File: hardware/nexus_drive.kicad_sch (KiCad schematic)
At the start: 0 parts

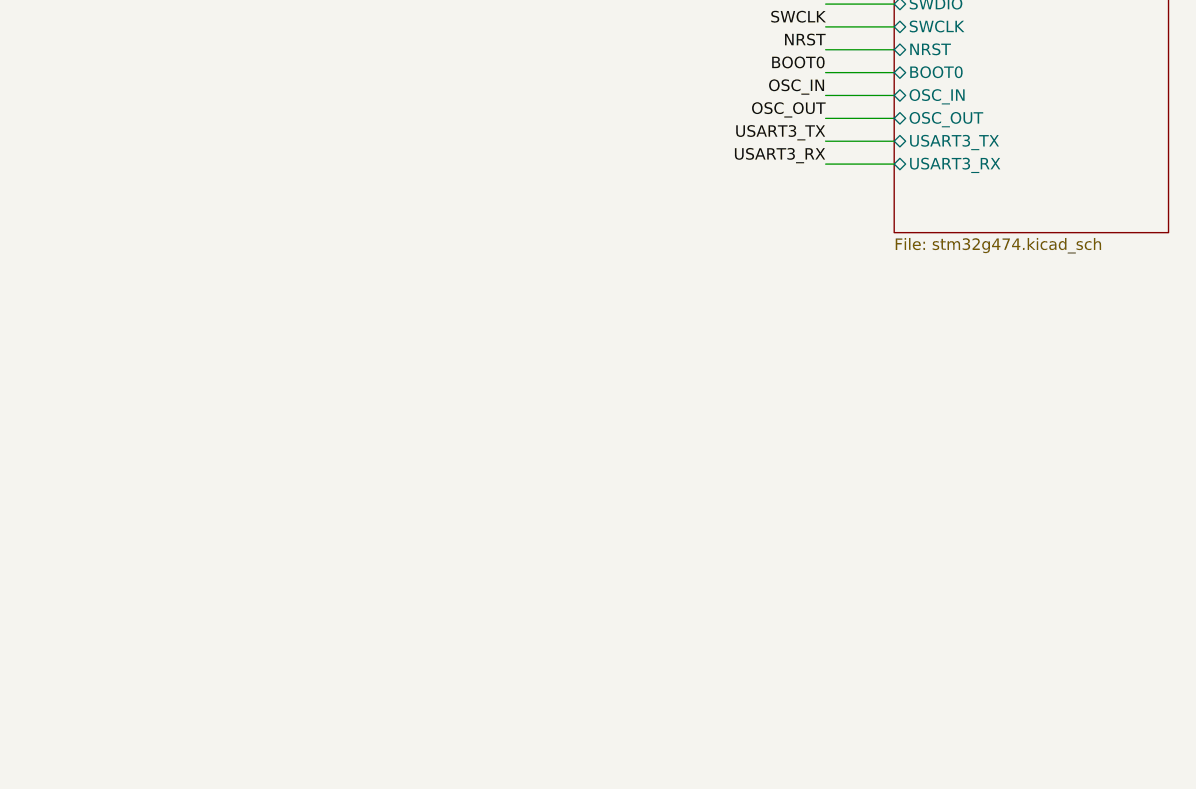
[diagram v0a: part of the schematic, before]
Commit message: Add CAN FD and encoder sheets; update MCU sheet and root schematic
Co-Authored-By: Claude Opus 5.5 <noreply@anthropic.com>
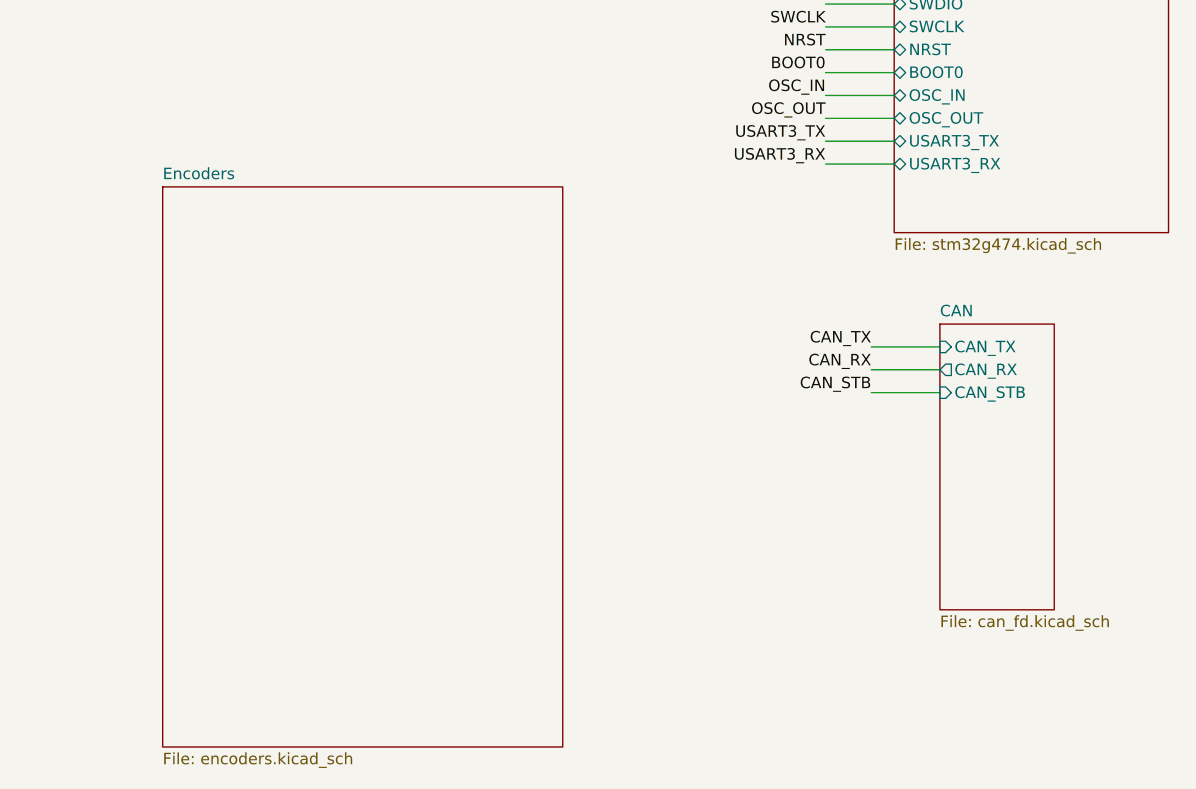
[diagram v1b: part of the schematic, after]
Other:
- added sheet CAN (can_fd.kicad_sch)
- added sheet Encoders (encoders.kicad_sch)

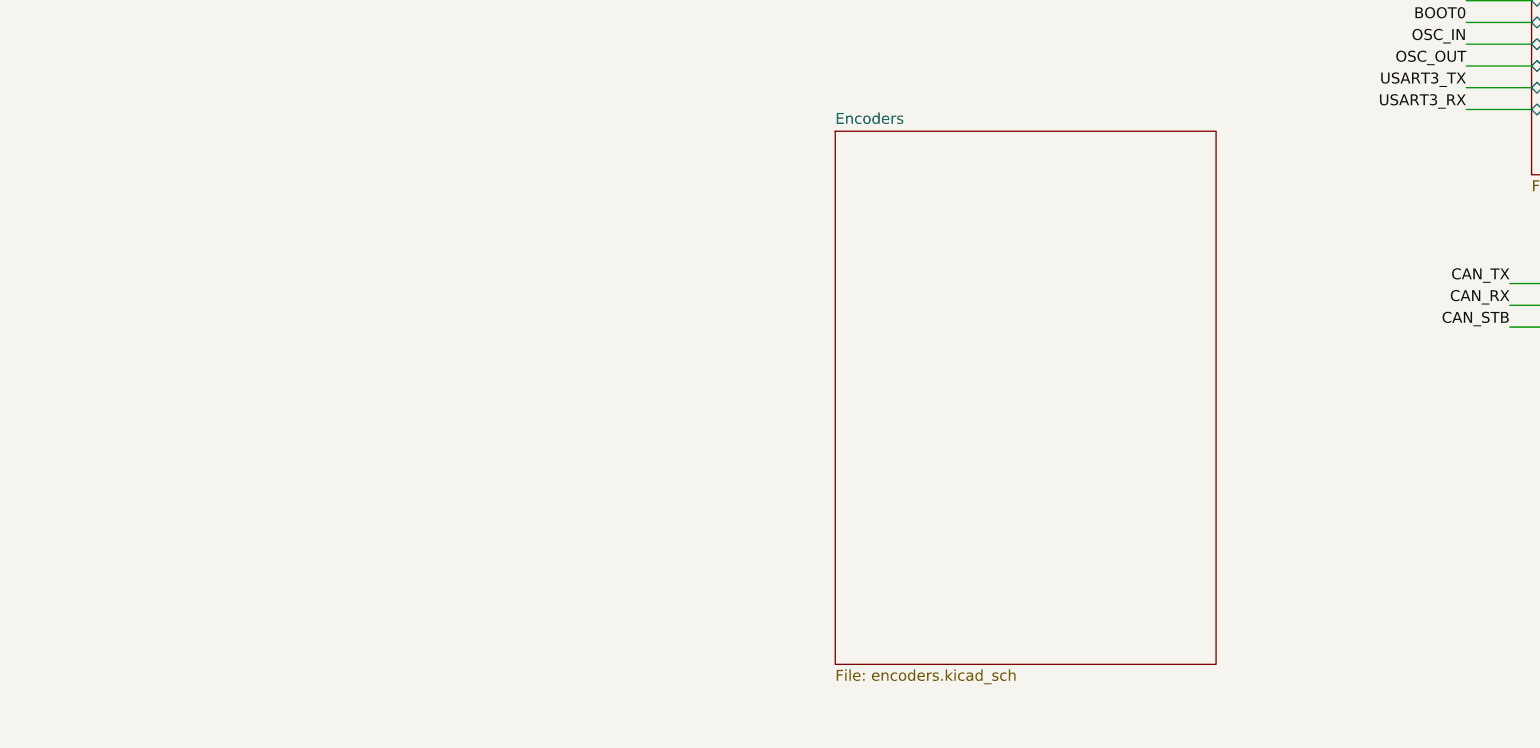
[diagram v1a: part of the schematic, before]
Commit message: Add sensing sheet; update MCU, CAN FD, encoder and root schematics
Co-Authored-By: Claude Opus 5.5 <noreply@anthropic.com>
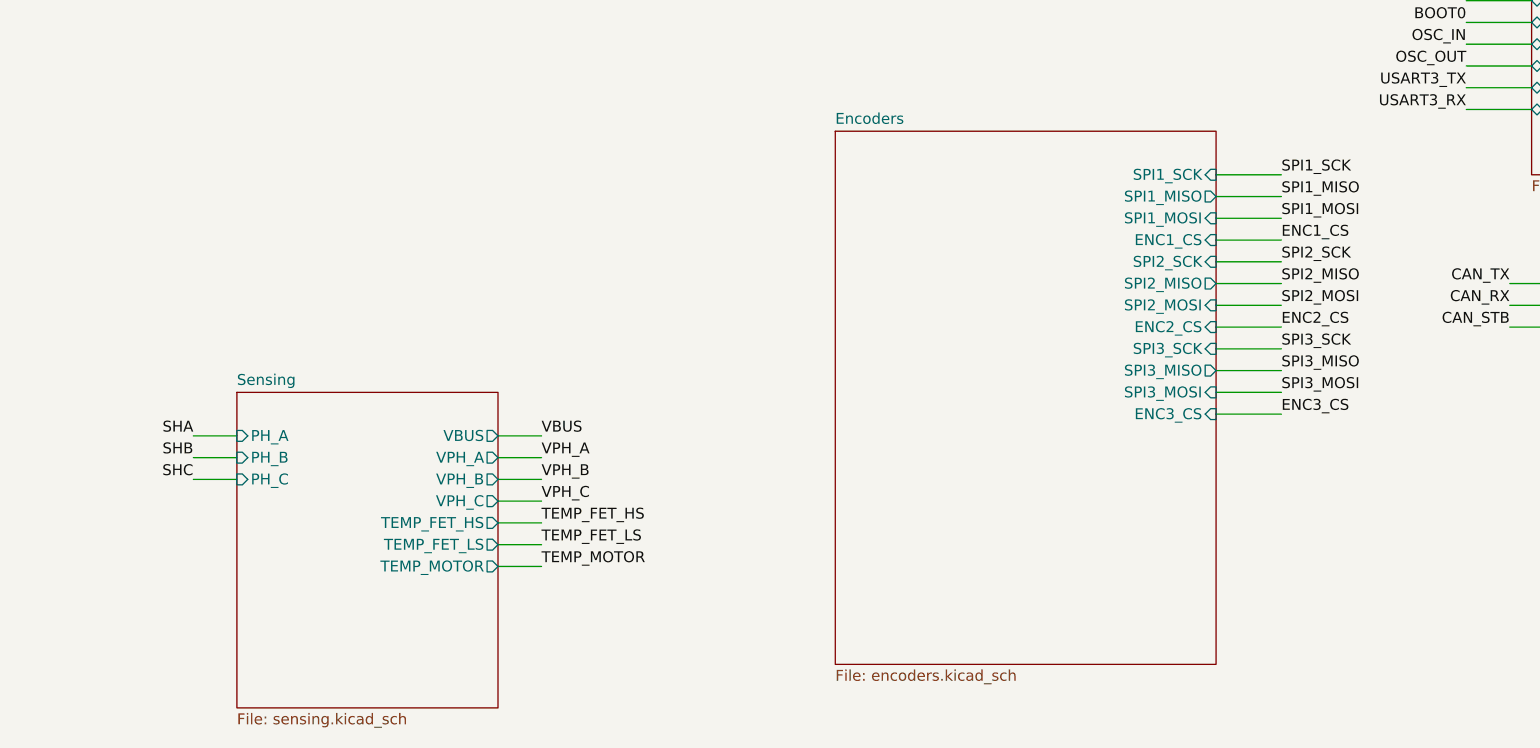
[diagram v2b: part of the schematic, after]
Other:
- added sheet Sensing (sensing.kicad_sch)
- sheet Encoders ports: added ENC1_CS, ENC2_CS, ENC3_CS, SPI1_MISO, SPI1_MOSI, SPI1_SCK, SPI2_MISO, SPI2_MOSI, SPI2_SCK, SPI3_MISO, SPI3_MOSI, SPI3_SCK; removed none

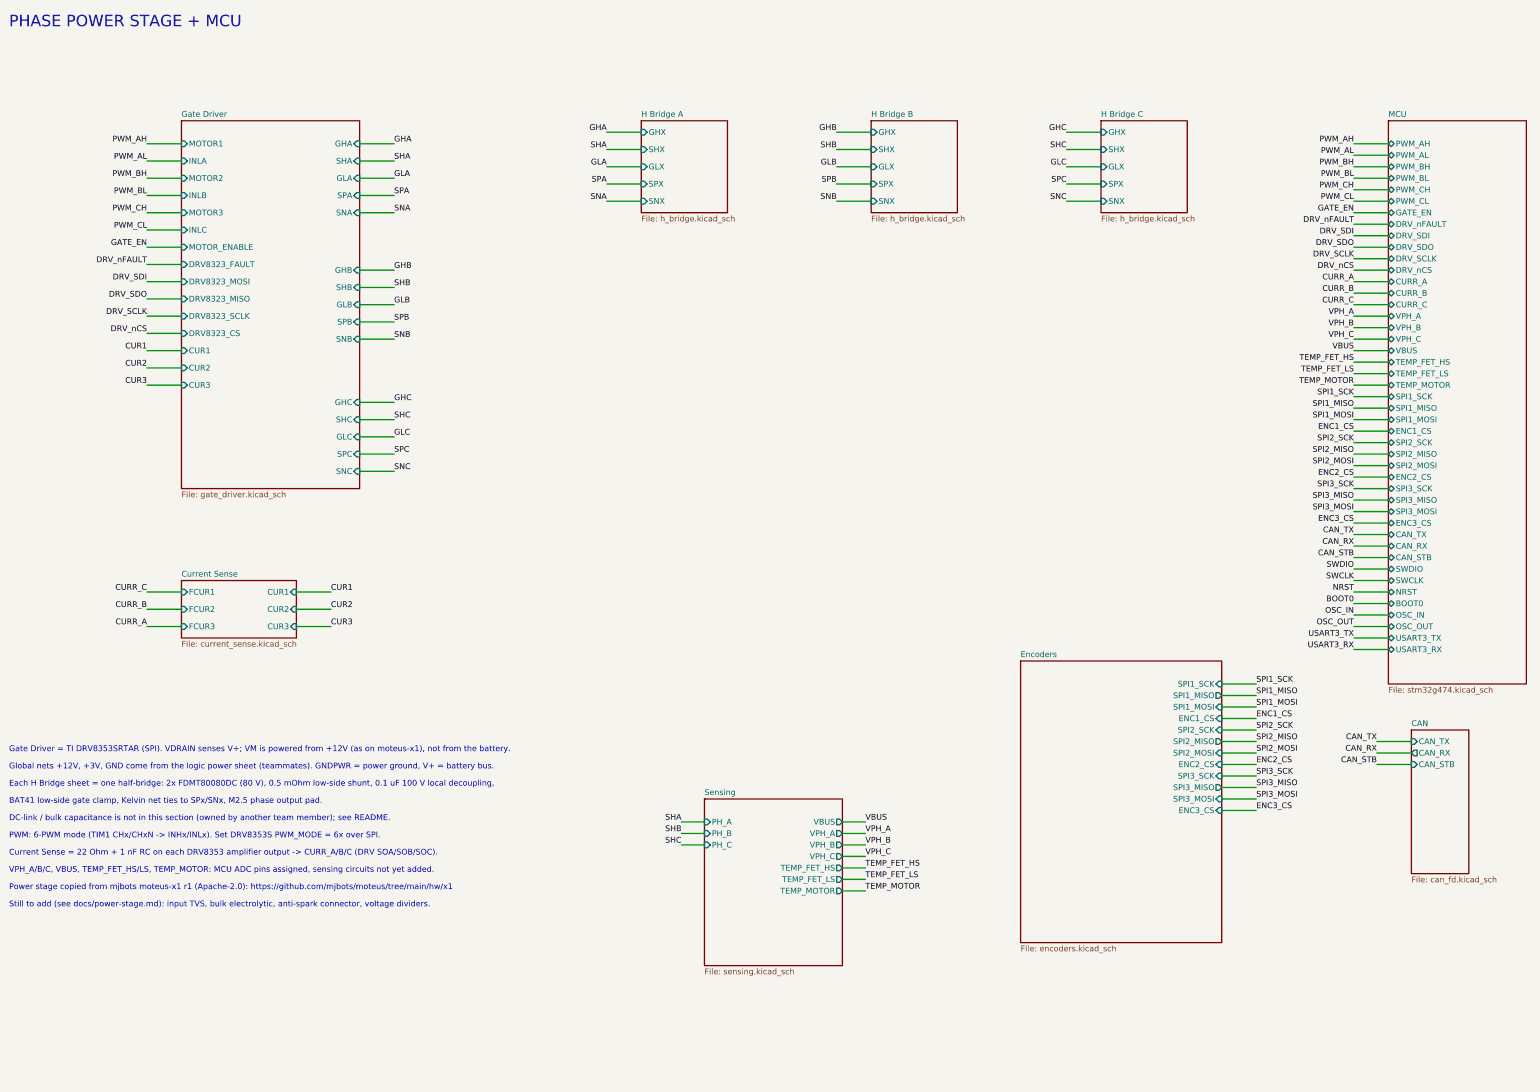
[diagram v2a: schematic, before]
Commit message: Clean up schematic ERC; add project symbol library; update README
Fix dangling labels, floating pins and pin types across the sheets so
ERC reports 0 errors (see hardware/CHANGES.txt). Add PWR_FLAGs and move
TCAN1042GV, MA702GQ and the EMI filter to nexus_drive.kicad_sym.

Update the README layout, specs and schematic review status.

Co-Authored-By: Claude Opus 5.5 <noreply@anthropic.com>
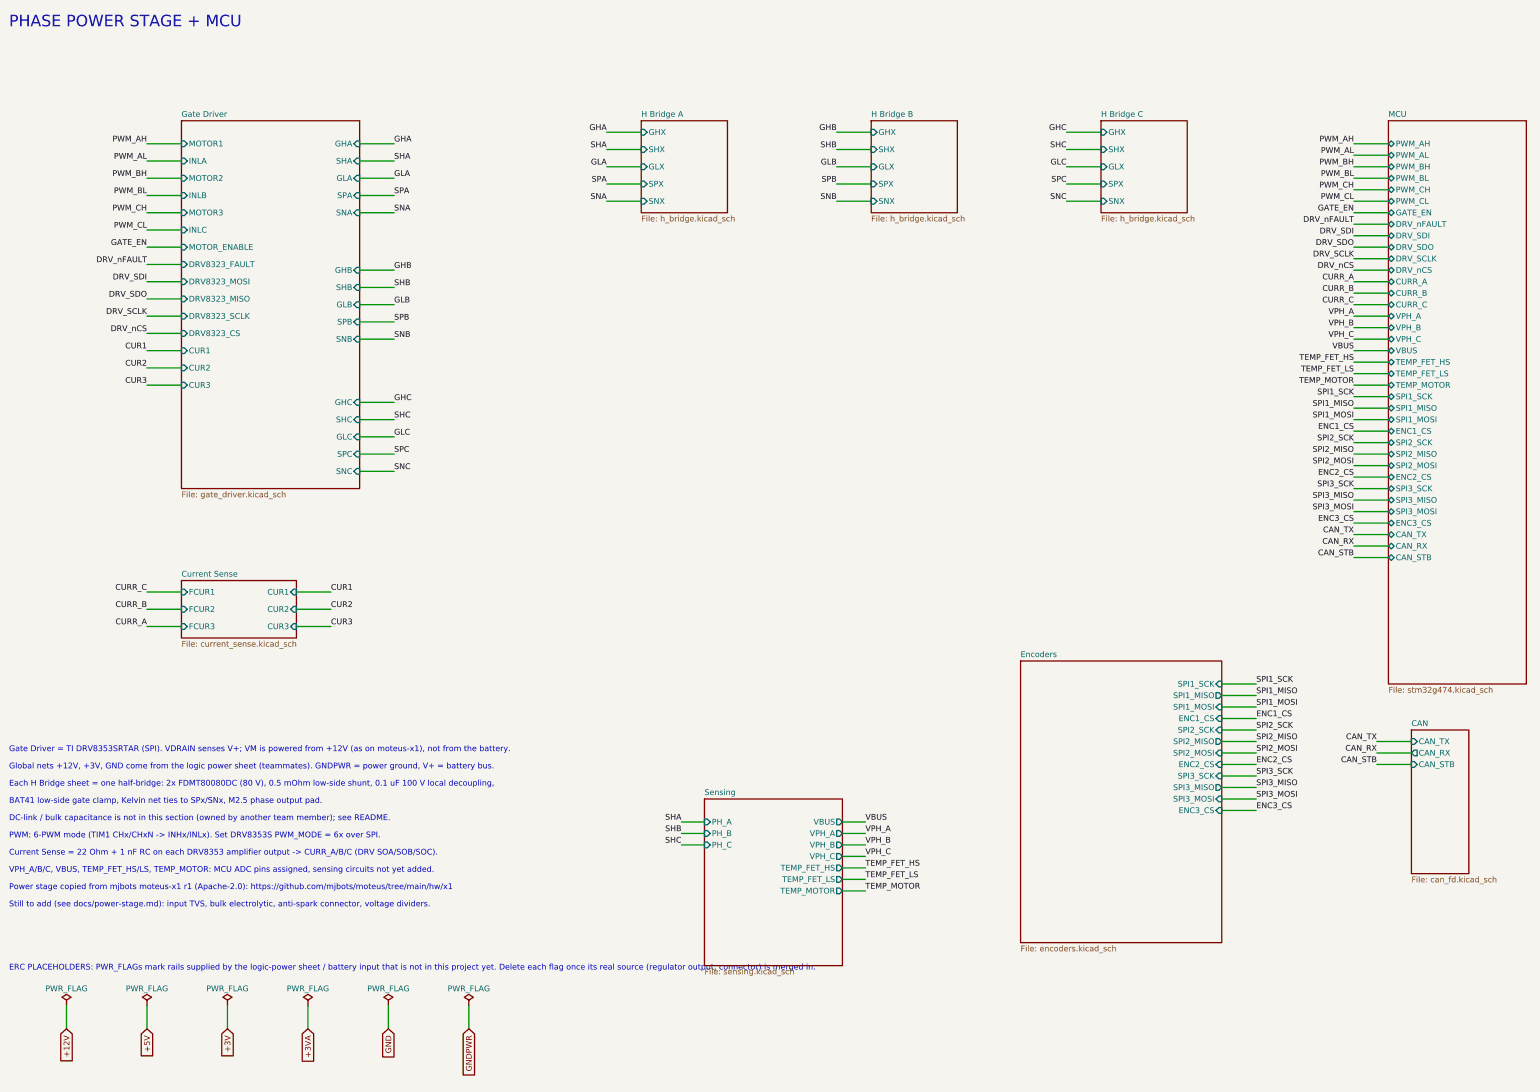
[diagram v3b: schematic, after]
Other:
- sheet MCU ports: added none; removed BOOT0, NRST, OSC_IN, OSC_OUT, SWCLK, SWDIO, USART3_RX, USART3_TX
- note added: "ERC PLACEHOLDERS: PWR_FLAGs mark rails supplied by the logic-power sheet / battery input that is not in this project yet. Delete each flag once its real source (regulator output, connector) is merged in."
